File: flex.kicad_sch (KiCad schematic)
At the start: 13 parts, among them Q3 AO3400A, Q4 AO3400A

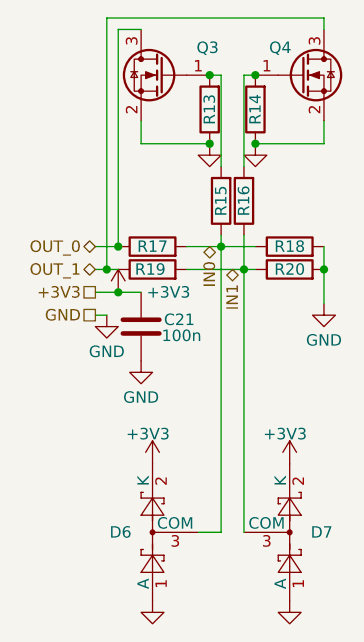
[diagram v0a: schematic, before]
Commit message: rest components placed
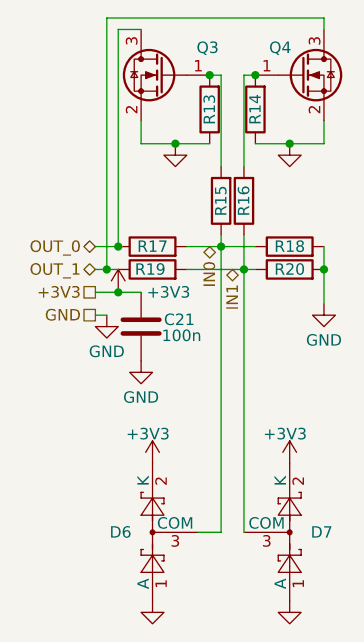
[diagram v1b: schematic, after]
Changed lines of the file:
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@@
-	)
-	(junction
-		(at 41.91 39.37)
-		(diameter 0)
-		(color 0 0 0 0)
-	)
-	(junction
-		(at 46.99 39.37)
-		(diameter 0)
-		(color 0 0 0 0)
 	)
 	(junction
@@
 	)
 	(junction
+		(at 38.1 39.37)
+		(diameter 0)
+		(color 0 0 0 0)
+	)
+	(junction
 		(at 43.18 50.8)
 		(diameter 0)
 		(color 0 0 0 0)
 	)
+	(junction
+		(at 50.8 39.37)
+		(diameter 0)
+		(color 0 0 0 0)
+	)
 	(wire
 		(pts
@@
 	(wire
 		(pts
+			(xy 50.8 39.37) (xy 46.99 39.37)
+		)
+		(stroke
+			(width 0)
+			(type default)
+		)
+	)
+	(wire
+		(pts
 			(xy 45.72 31.75) (xy 45.72 41.91)
 		)
@@
 	(wire
 		(pts
+			(xy 38.1 39.37) (xy 41.91 39.37)
+		)
+		(stroke
+			(width 0)
+			(type default)
+		)
+	)
+	(wire
+		(pts
 			(xy 30.48 25.4) (xy 30.48 53.34)
 		)
@@
 	(wire
 		(pts
-			(xy 54.61 39.37) (xy 46.99 39.37)
-		)
-		(stroke
-			(width 0)
-			(type default)
-		)
-	)
-	(wire
-		(pts
-			(xy 34.29 39.37) (xy 41.91 39.37)
+			(xy 54.61 39.37) (xy 50.8 39.37)
+		)
+		(stroke
+			(width 0)
+			(type default)
+		)
+	)
+	(wire
+		(pts
+			(xy 34.29 39.37) (xy 38.1 39.37)
 		)
 		(stroke
@@
 	(symbol
 		(lib_id "power:GND")
-		(at 41.91 39.37 0)
+		(at 38.1 39.37 0)
 		(unit 1)
 		(exclude_from_sim no)
@@
 		(dnp no)
 		(property "Reference" "#PWR068"
-			(at 41.91 45.72 0)
+			(at 38.1 45.72 0)
 			(effects
 				(font
@@
 		)
 		(property "Value" "GND"
-			(at 55.372 41.402 0)
+			(at 51.562 41.402 0)
 			(effects
 				(font
@@
 		)
 		(property "Footprint" ""
-			(at 41.91 39.37 0)
+			(at 38.1 39.37 0)
 			(effects
 				(font
@@
 		)
 		(property "Datasheet" ""
-			(at 41.91 39.37 0)
+			(at 38.1 39.37 0)
 			(effects
 				(font
@@
 		)
 		(property "Description" "Power symbol creates a global label with name \"GND\" , ground"
-			(at 41.91 39.37 0)
+			(at 38.1 39.37 0)
 			(effects
 				(font
@@
 	(symbol
 		(lib_id "power:GND")
-		(at 46.99 39.37 0)
+		(at 50.8 39.37 0)
 		(unit 1)
 		(exclude_from_sim no)
@@
 		(dnp no)
 		(property "Reference" "#PWR069"
-			(at 46.99 45.72 0)
+			(at 50.8 45.72 0)
 			(effects
 				(font
@@
 		)
 		(property "Value" "GND"
-			(at 60.452 41.402 0)
+			(at 64.262 41.402 0)
 			(effects
 				(font
@@
 		)
 		(property "Footprint" ""
-			(at 46.99 39.37 0)
+			(at 50.8 39.37 0)
 			(effects
 				(font
@@
 		)
 		(property "Datasheet" ""
-			(at 46.99 39.37 0)
+			(at 50.8 39.37 0)
 			(effects
 				(font
@@
 		)
 		(property "Description" "Power symbol creates a global label with name \"GND\" , ground"
-			(at 46.99 39.37 0)
-			(effects
-				(font
+			(at 50.8 39.37 0)
+			(effects
+				(font

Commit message: review passed
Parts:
- C21: value 100n -> 100nF
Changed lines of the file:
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@@
 			)
 		)
-		(property "Value" "100n"
+		(property "Value" "100nF"
 			(at 36.576 60.706 0)
 			(effects
